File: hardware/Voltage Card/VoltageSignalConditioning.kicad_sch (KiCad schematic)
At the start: 4 parts

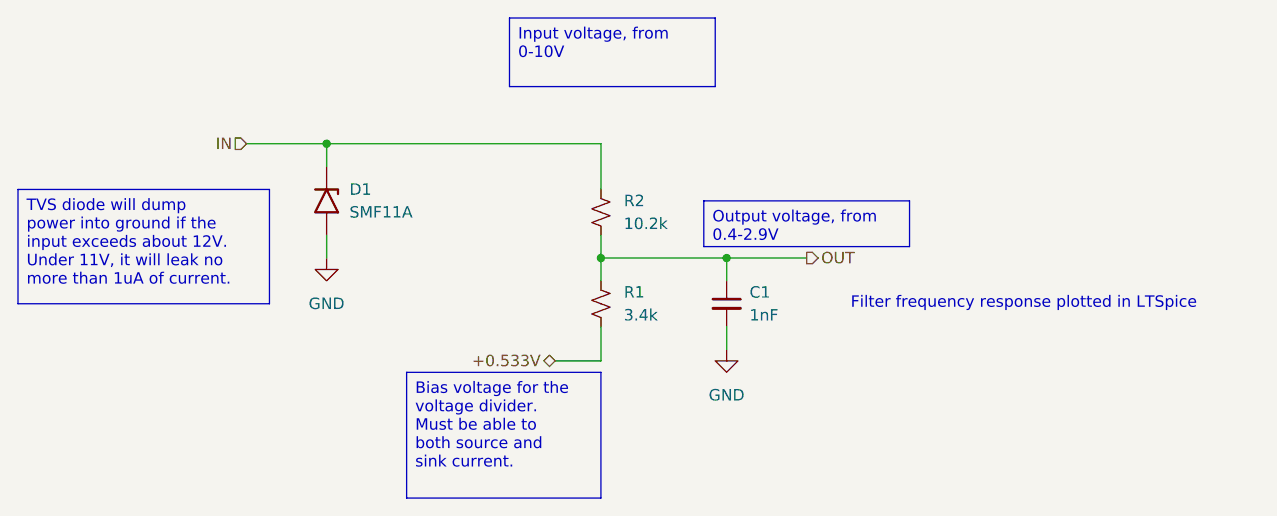
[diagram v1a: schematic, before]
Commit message: Update voltage card to KiCAD 10
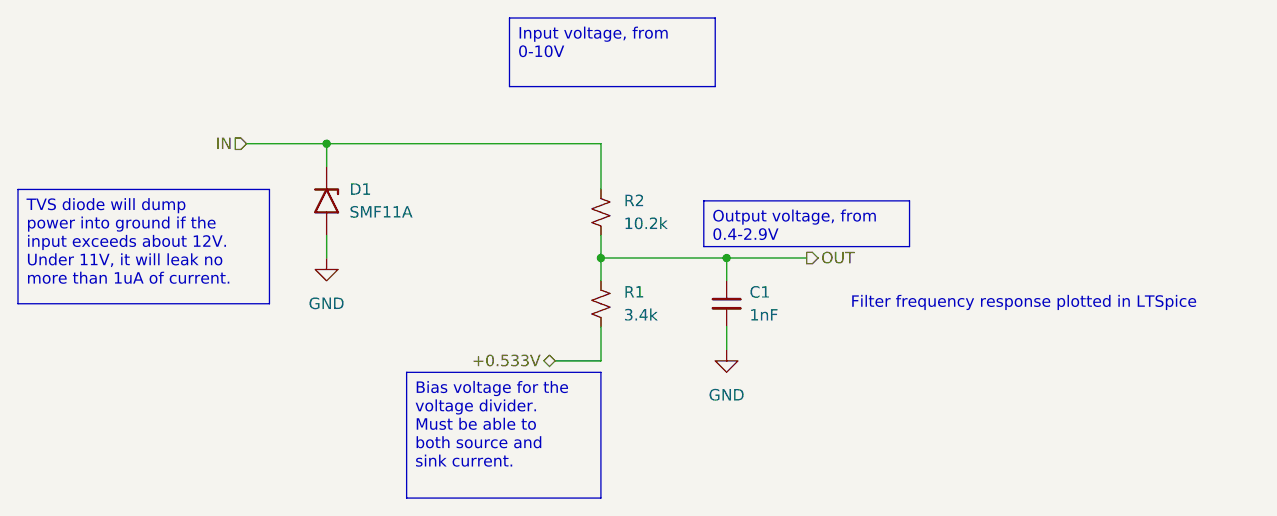
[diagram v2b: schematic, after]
